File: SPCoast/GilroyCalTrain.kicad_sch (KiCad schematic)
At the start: 95 parts, among them SW3771 771, SW3773 773, SW3775 775

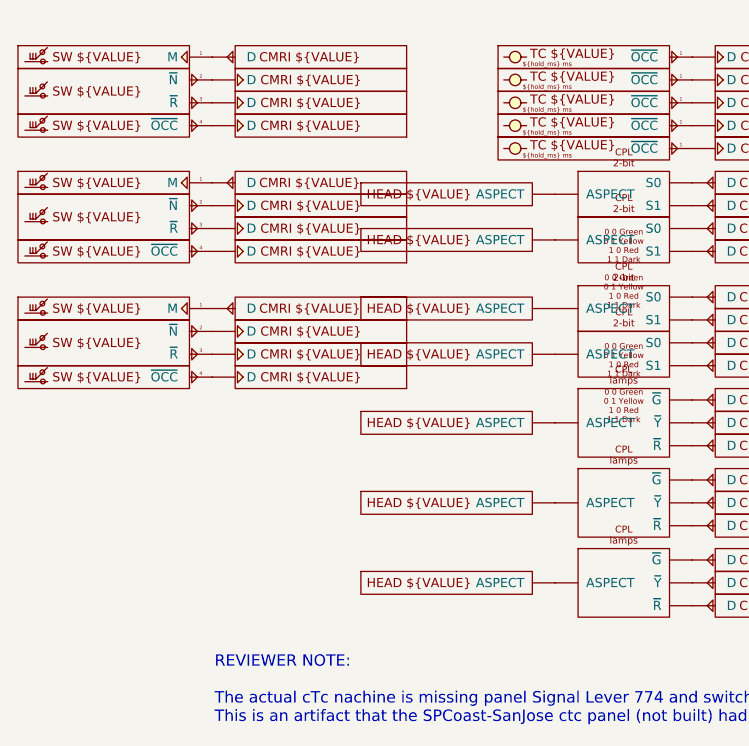
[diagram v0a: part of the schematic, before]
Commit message: refactor(kicad): mast anchors with explicit indication-to-aspect casts; restore fields KiCad reset
Second pass after the cast chains (b4c58d3), decided 2026-10-17: the per-head
anchors Head-CPL/CL/Semaphore were the mast's indication table collapsed into
a symbol. The chain is now

    [Mast 774NAB] -indication- [Cast-Aspect-CPL unit B] -aspect- [Cast-Encoder-CPL] -bits- [chip]

Cast-Aspect-CPL/CL/Semaphore are multi-unit casts, one unit per head letter
(A..E), so placing unit B beside mast 774N is head 774NB with nothing typed;
the reader derives every head name from mast plus unit. Style's home is the
aspect cast. The project ERC now ignores missing_unit and missing_input_pin,
since an aspect cast places only the units its mast has.

CMRI bits: Address is the node (the chip every bit folds into, as for every
other driver), Bit is the bit, UA = ${Address} is a display echo, Value =
UA${Address}.IN.${Bit}.

Restore (SPCoast/edits/2026-10-17-restore-reset-fields.py): the owner's last
KiCad save before 857cae2 ran "update symbols from library" with field reset,
putting library defaults into per-instance fields on nine sheets: every
PanelLamp IndicationToken ("S"), PanelColumn Interlocking ("Luchessa"),
Luchessa encoding Station ("Panel"), Sargent Exp2 PCA9685-PWM 0x27 -> 0x20
(colliding with Exp3), and the 34 Caltrain bit numbers. All 98 values are
restored from the last good netlist export, embedded in the script.

Scripts: SPCoast/edits/2026-10-17-mast-chain.py (second pass; reuses the
first pass's helpers), 2026-10-17-restore-reset-fields.py. __pycache__/
added to .gitignore.

Verified:
- post-restore netlist vs the last good export: no field differs except on
  the anchors the first pass replaced and the intended JMRI blanks
- lint_symbol_fields: 93 symbols, 0 errors (per-unit cast rule)
- kicad-cli ERC: 0 violations; netlist export without warnings
- gate vs post-restore: nets not touching an anchor identical; all 11 aspect
  nets re-sourced from a Cast-Aspect un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
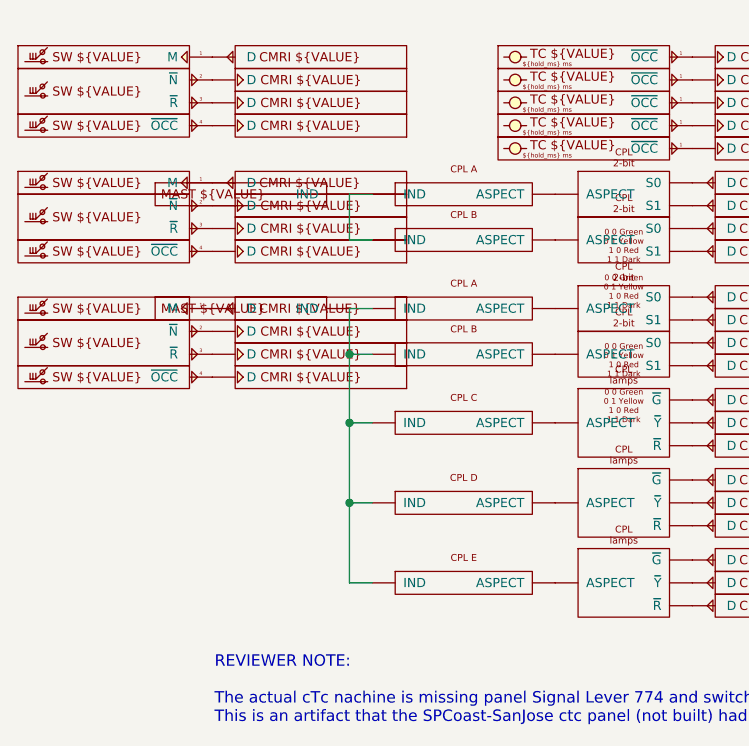
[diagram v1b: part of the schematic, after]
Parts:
- removed DevHead10: 774ND, symbol Railroad-Field:Head-CPL
- removed DevHead11: 774NE, symbol Railroad-Field:Head-CPL
- removed DevHead5: 774SA, symbol Railroad-Field:Head-CPL
- removed DevHead6: 774SB, symbol Railroad-Field:Head-CPL
- removed DevHead7: 774NA, symbol Railroad-Field:Head-CPL
- removed DevHead8: 774NB, symbol Railroad-Field:Head-CPL
- removed DevHead9: 774NC, symbol Railroad-Field:Head-CPL
- added Cast16, Cast17: (no value), symbol Railroad-Field:Cast-Aspect-CPL
- added DevMast3: 774N, symbol Railroad-Field:Mast
- added DevMast4: 774S, symbol Railroad-Field:Mast
- CMRI1: value UA${UA}.OUT.${ADDRESS} -> UA${Address}.OUT.${Bit}; Address 1 -> 30; Bit (none) -> 1; UA 30 -> ${Address}
- CMRI10: value UA${UA}.IN.${ADDRESS} -> UA${Address}.IN.${Bit}; Address 1 -> 30; Bit (none) -> 7; UA 30 -> ${Address}
- CMRI11: value UA${UA}.IN.${ADDRESS} -> UA${Address}.IN.${Bit}; Address 1 -> 30; Bit (none) -> 8; UA 30 -> ${Address}
- CMRI12: value UA${UA}.IN.${ADDRESS} -> UA${Address}.IN.${Bit}; Address 1 -> 30; Bit (none) -> 9; UA 30 -> ${Address}
- CMRI13: value UA${UA}.IN.${ADDRESS} -> UA${Address}.IN.${Bit}; Address 1 -> 30; Bit (none) -> 10; UA 30 -> ${Address}
- CMRI14: value UA${UA}.IN.${ADDRESS} -> UA${Address}.IN.${Bit}; Address 1 -> 30; Bit (none) -> 11; UA 30 -> ${Address}
- CMRI15: value UA${UA}.IN.${ADDRESS} -> UA${Address}.IN.${Bit}; Address 1 -> 30; Bit (none) -> 12; UA 30 -> ${Address}
- CMRI16: value UA${UA}.IN.${ADDRESS} -> UA${Address}.IN.${Bit}; Address 1 -> 30; Bit (none) -> 13; UA 30 -> ${Address}
- CMRI17: value UA${UA}.IN.${ADDRESS} -> UA${Address}.IN.${Bit}; Address 1 -> 30; Bit (none) -> 14; UA 30 -> ${Address}
- CMRI18: value UA${UA}.OUT.${ADDRESS} -> UA${Address}.OUT.${Bit}; Address 1 -> 30; Bit (none) -> 4; UA 30 -> ${Address}
- CMRI19: value UA${UA}.OUT.${ADDRESS} -> UA${Address}.OUT.${Bit}; Address 1 -> 30; Bit (none) -> 5; UA 30 -> ${Address}
- CMRI2: value UA${UA}.IN.${ADDRESS} -> UA${Address}.IN.${Bit}; Address 1 -> 30; Bit (none) -> 1; UA 30 -> ${Address}
- CMRI20: value UA${UA}.OUT.${ADDRESS} -> UA${Address}.OUT.${Bit}; Address 1 -> 30; Bit (none) -> 6; UA 30 -> ${Address}
- CMRI21: value UA${UA}.OUT.${ADDRESS} -> UA${Address}.OUT.${Bit}; Address 1 -> 30; Bit (none) -> 7; UA 30 -> ${Address}
- CMRI22: value UA${UA}.OUT.${ADDRESS} -> UA${Address}.OUT.${Bit}; Address 1 -> 30; Bit (none) -> 8; UA 30 -> ${Address}
- CMRI23: value UA${UA}.OUT.${ADDRESS} -> UA${Address}.OUT.${Bit}; Address 1 -> 30; Bit (none) -> 9; UA 30 -> ${Address}
- CMRI24: value UA${UA}.OUT.${ADDRESS} -> UA${Address}.OUT.${Bit}; Address 1 -> 30; Bit (none) -> 10; UA 30 -> ${Address}
- CMRI25: value UA${UA}.OUT.${ADDRESS} -> UA${Address}.OUT.${Bit}; Address 1 -> 30; Bit (none) -> 11; UA 30 -> ${Address}
- CMRI26: value UA${UA}.OUT.${ADDRESS} -> UA${Address}.OUT.${Bit}; Address 1 -> 30; Bit (none) -> 12; UA 30 -> ${Address}
- CMRI27: value UA${UA}.OUT.${ADDRESS} -> UA${Address}.OUT.${Bit}; Address 1 -> 30; Bit (none) -> 13; UA 30 -> ${Address}
- CMRI28: value UA${UA}.OUT.${ADDRESS} -> UA${Address}.OUT.${Bit}; Address 1 -> 30; Bit (none) -> 14; UA 30 -> ${Address}
- CMRI29: value UA${UA}.OUT.${ADDRESS} -> UA${Address}.OUT.${Bit}; Address 1 -> 30; Bit (none) -> 15; UA 30 -> ${Address}
- CMRI3: value UA${UA}.IN.${ADDRESS} -> UA${Address}.IN.${Bit}; Address 1 -> 30; Bit (none) -> 2; UA 30 -> ${Address}
- CMRI30: value UA${UA}.OUT.${ADDRESS} -> UA${Address}.OUT.${Bit}; Address 1 -> 30; Bit (none) -> 16; UA 30 -> ${Address}
- CMRI31: value UA${UA}.OUT.${ADDRESS} -> UA${Address}.OUT.${Bit}; Address 1 -> 30; Bit (none) -> 17; UA 30 -> ${Address}
- CMRI32: value UA${UA}.OUT.${ADDRESS} -> UA${Address}.OUT.${Bit}; Address 1 -> 30; Bit (none) -> 18; UA 30 -> ${Address}
- CMRI33: value UA${UA}.OUT.${ADDRESS} -> UA${Address}.OUT.${Bit}; Address 1 -> 30; Bit (none) -> 19; UA 30 -> ${Address}
- CMRI34: value UA${UA}.OUT.${ADDRESS} -> UA${Address}.OUT.${Bit}; Address 1 -> 30; Bit (none) -> 20; UA 30 -> ${Address}
- CMRI4: value UA${UA}.IN.${ADDRESS} -> UA${Address}.IN.${Bit}; Address 1 -> 30; Bit (none) -> 3; UA 30 -> ${Address}
- CMRI5: value UA${UA}.OUT.${ADDRESS} -> UA${Address}.OUT.${Bit}; Address 1 -> 30; Bit (none) -> 2; UA 30 -> ${Address}
- CMRI6: value UA${UA}.IN.${ADDRESS} -> UA${Address}.IN.${Bit}; Address 1 -> 30; Bit (none) -> 4; UA 30 -> ${Address}
- CMRI7: value UA${UA}.IN.${ADDRESS} -> UA${Address}.IN.${Bit}; Address 1 -> 30; Bit (none) -> 5; UA 30 -> ${Address}
- CMRI8: value UA${UA}.IN.${ADDRESS} -> UA${Address}.IN.${Bit}; Address 1 -> 30; Bit (none) -> 6; UA 30 -> ${Address}
- CMRI9: value UA${UA}.OUT.${ADDRESS} -> UA${Address}.OUT.${Bit}; Address 1 -> 30; Bit (none) -> 3; UA 30 -> ${Address}
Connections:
- net at Cast8.3 (ASPECT): now also Cast16.2 (ASPECT)
- net at Cast7.4 (ASPECT): now also Cast16.6 (ASPECT)
- net at Cast9.4 (ASPECT): now also Cast16.10 (ASPECT)
- net at Cast10.3 (ASPECT): now also Cast17.4 (ASPECT)
- net at Cast12.3 (ASPECT): now also Cast17.2 (ASPECT)
- net at Cast6.4 (ASPECT): now also Cast16.8 (ASPECT)
- net at Cast11.3 (ASPECT): now also Cast16.4 (ASPECT)
- new net: Cast17.1 (IND), Cast17.3 (IND), DevMast4.1 (IND)
- new net: Cast16.1 (IND), Cast16.3 (IND), Cast16.5 (IND), Cast16.7 (IND), Cast16.9 (IND), DevMast3.1 (IND)

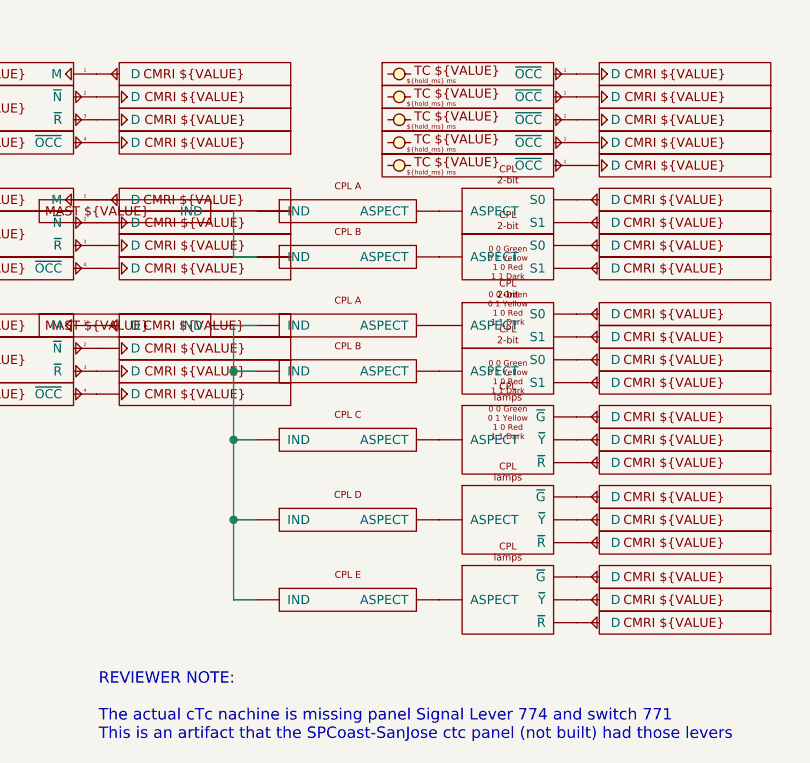
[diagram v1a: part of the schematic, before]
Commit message: refactor(kicad): one-step head casts with an explicit Head letter
The multi-unit aspect casts hid the head assignment in a KiCad unit number
and said the head style twice. One cast per head rendering now takes the
mast's indication and drives the lamps, select code, LED, color point or
arm directly: Cast-Head-CPL, Cast-Head-CPL-Encoded, Cast-Head-RGB,
Cast-Head-Color, Cast-Head-Semaphore (Role CAST, IND input, shown Head and
Style fields). The aspect is derived from style and indication, never
drawn; the aspect pin kind is retired. Cast-Aspect-*, Cast-Lamps-*,
Cast-Encoder-CPL, Cast-Color and Cast-Arm are retired. Bodies follow the
owner's tidy: one width, visible text inside, Pin.* beside their pins, the
encoder's select-code table kept. Two renderings of one head (836SB: arm
and RGB LED) are two casts with the same Head on the mast's IND net.

Sargent and GilroyCalTrain: every unit and its downstream casts collapse
onto the downstream positions by 2026-10-18-head-cast.py, pairing by the
baseline netlist; the ERC severities set to ignore for partial multi-unit
placement go back to warning.

Verified: 2026-10-18-head-cast-gate.py on production/pre-head.net vs
post-head.net: 535 nets not touching a unit or a head input identical;
eleven head names derived from mast Value + Head equal the old unit
letters (774NA-E, 774SA-B, 836NA-B, 836SA-B); only the 12 head casts
re-symbolled; no field change outside their own fields; ERC 0;
lint_symbol_fields 90 symbols 0 errors; sync-library-fields changed 0.

Co-Authored-By: Claude Fable 5.1 <noreply@anthropic.com>
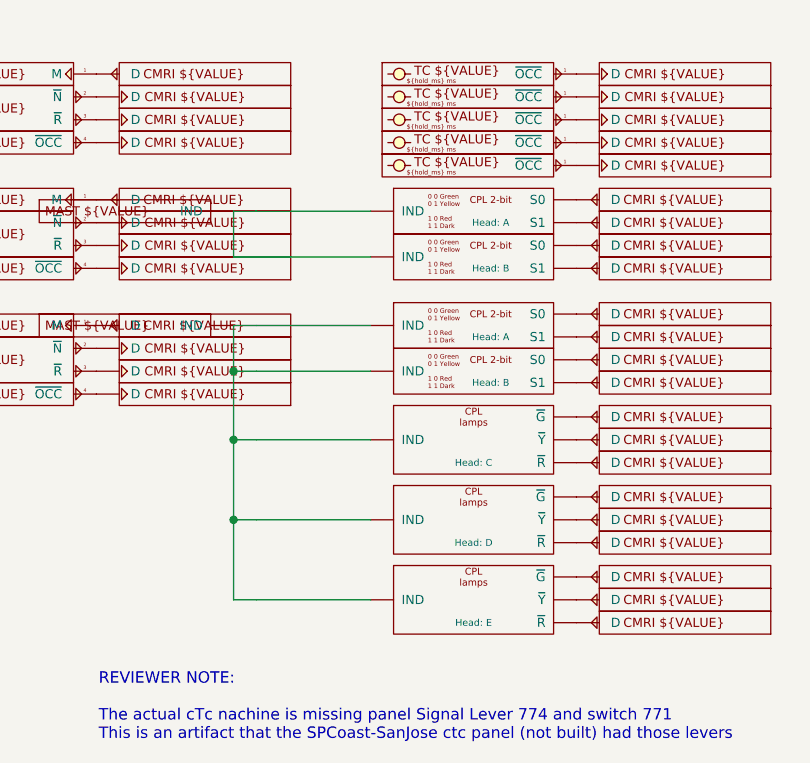
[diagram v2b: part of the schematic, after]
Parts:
- removed Cast10, Cast11, Cast12, Cast8: (no value), symbol Railroad-Field:Cast-Encoder-CPL
- removed Cast16, Cast17: (no value), symbol Railroad-Field:Cast-Aspect-CPL
- removed Cast6, Cast7, Cast9: (no value), symbol Railroad-Field:Cast-Lamps-RYG
- added Cast10, Cast11, Cast12, Cast8: (no value), symbol Railroad-Field:Cast-Head-CPL-Encoded
- added Cast6, Cast7, Cast9: (no value), symbol Railroad-Field:Cast-Head-CPL
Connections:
- net at CMRI22.1 (D): now also Cast8.1 (S0)
- net at CMRI18.1 (D): now also Cast12.1 (S0)
- net at CMRI23.1 (D): now also Cast8.2 (S1)
- net at CMRI26.1 (D): now also Cast7.1 (~{G})
- net at CMRI27.1 (D): now also Cast7.2 (~{Y})
- net at CMRI28.1 (D): now also Cast7.3 (~{R})
- net at CMRI24.1 (D): now also Cast11.1 (S0)
- net at CMRI20.1 (D): now also Cast10.1 (S0)
- net at CMRI21.1 (D): now also Cast10.2 (S1)
- net at CMRI19.1 (D): now also Cast12.2 (S1)
- net at DevMast4.1 (IND): now also Cast10.3 (IND), Cast12.3 (IND)
- net at CMRI33.1 (D): now also Cast9.2 (~{Y})
- net at DevMast3.1 (IND): now also Cast11.3 (IND), Cast6.4 (IND), Cast7.4 (IND), Cast8.3 (IND), Cast9.4 (IND)
- net at CMRI32.1 (D): now also Cast9.1 (~{G})
- net at CMRI31.1 (D): now also Cast6.3 (~{R})
- net at CMRI34.1 (D): now also Cast9.3 (~{R})
- net at CMRI25.1 (D): now also Cast11.2 (S1)
- net at CMRI29.1 (D): now also Cast6.1 (~{G})
- net at CMRI30.1 (D): now also Cast6.2 (~{Y})
